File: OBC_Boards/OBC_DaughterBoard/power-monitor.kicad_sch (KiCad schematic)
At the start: 5 parts

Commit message: temp sensor footprint
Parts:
- TP2: renamed from TP?; footprint (none) -> TestPoint:TestPoint_2Pads_Pitch2.54mm_Drill0.8mm
- gave numbers to parts that had none: 4
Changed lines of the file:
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@@
   (symbol (lib_id "STM32_Breakout-rescue:MAX4372FESA+-MAX4372FESA+") (at 116.84 68.453 0) (unit 1)
     (in_bom yes) (on_board yes)
-    (property "Reference" "MAX4372F?" (id 0) (at 144.78 58.6232 0)
+    (property "Reference" "MAX4372F2" (id 0) (at 144.78 58.6232 0)
       (effects (font (size 1.524 1.524)))
     )
@@
   (symbol (lib_id "Imported_OBC_Library:+3.3V") (at 176.53 81.153 0) (mirror x) (unit 1)
     (in_bom yes) (on_board yes) (fields_autoplaced)
-    (property "Reference" "#PWR?" (id 0) (at 176.53 77.343 0)
+    (property "Reference" "#PWR0139" (id 0) (at 176.53 77.343 0)
       (effects (font (size 1.27 1.27)) hide)
     )
@@
   (symbol (lib_id "Device:R") (at 184.785 71.755 0) (unit 1)
     (in_bom yes) (on_board yes) (fields_autoplaced)
-    (property "Reference" "R?" (id 0) (at 187.325 70.4849 0)
+    (property "Reference" "R12" (id 0) (at 187.325 70.4849 0)
       (effects (font (size 1.27 1.27)) (justify left))
     )
@@
   (symbol (lib_id "power:GND") (at 141.605 127 0) (unit 1)
     (in_bom yes) (on_board yes)
-    (property "Reference" "#PWR?" (id 0) (at 141.605 133.35 0)
+    (property "Reference" "#PWR0128" (id 0) (at 141.605 133.35 0)
       (effects (font (size 1.27 1.27)) hide)
     )
@@
   (symbol (lib_id "Connector:TestPoint") (at 176.53 80.391 90) (unit 1)
     (in_bom yes) (on_board yes)
-    (property "Reference" "TP?" (id 0) (at 172.212 84.455 90)
+    (property "Reference" "TP2" (id 0) (at 172.212 84.455 90)
       (effects (font (size 1.27 1.27)) (justify left))
     )
@@
       (effects (font (size 1.27 1.27)) (justify left))
     )
-    (property "Footprint" "" (id 2) (at 176.53 75.311 0)
+    (property "Footprint" "TestPoint:TestPoint_2Pads_Pitch2.54mm_Drill0.8mm" (id 2) (at 176.53 75.311 0)
       (effects (font (size 1.27 1.27)) hide)
     )
@@
   (symbol (lib_id "Device:FerriteBead_Small") (at 91.44 68.58 270) (unit 1)
     (in_bom yes) (on_board yes)
-    (property "Reference" "FB?" (id 0) (at 89.535 62.865 90))
+    (property "Reference" "FB5" (id 0) (at 89.535 62.865 90))
     (property "Value" "100R @ 100 MHz" (id 1) (at 95.885 65.405 90))
     (property "Footprint" "Daughterboard_footprints:BEADC1608X75N" (id 2) (at 91.44 66.802 90)
@@
   (symbol (lib_id "Imported_OBC_Library:+3.3V") (at 133.985 94.615 0) (unit 1)
     (in_bom yes) (on_board yes)
-    (property "Reference" "#PWR?" (id 0) (at 133.985 98.425 0)
+    (property "Reference" "#PWR0132" (id 0) (at 133.985 98.425 0)
       (effects (font (size 1.27 1.27)) hide)
     )
@@
   (symbol (lib_id "power:GND") (at 133.985 127 0) (unit 1)
     (in_bom yes) (on_board yes)
-    (property "Reference" "#PWR?" (id 0) (at 133.985 133.35 0)
+    (property "Reference" "#PWR0127" (id 0) (at 133.985 133.35 0)
       (effects (font (size 1.27 1.27)) hide)
     )
@@
   (symbol (lib_id "Analog_ADC:MCP3008") (at 136.525 109.855 0) (unit 1)
     (in_bom yes) (on_board yes)
-    (property "Reference" "U?" (id 0) (at 110.109 112.141 0)
+    (property "Reference" "U5" (id 0) (at 110.109 112.141 0)
       (effects (font (size 1.27 1.27)) (justify left))
     )
@@
   (symbol (lib_id "power:GND") (at 107.95 79.375 0) (unit 1)
     (in_bom yes) (on_board yes)
-    (property "Reference" "#PWR?" (id 0) (at 107.95 85.725 0)
+    (property "Reference" "#PWR0137" (id 0) (at 107.95 85.725 0)
       (effects (font (size 1.27 1.27)) hide)
     )
@@
   (symbol (lib_id "Imported_OBC_Library:+3.3V") (at 86.995 59.69 0) (unit 1)
     (in_bom yes) (on_board yes)
-    (property "Reference" "#PWR?" (id 0) (at 86.995 63.5 0)
+    (property "Reference" "#PWR0138" (id 0) (at 86.995 63.5 0)
       (effects (font (size 1.27 1.27)) hide)
     )
@@
   (symbol (lib_id "Imported_OBC_Library:+3.3V") (at 141.605 94.615 0) (unit 1)
     (in_bom yes) (on_board yes)
-    (property "Reference" "#PWR?" (id 0) (at 141.605 98.425 0)
+    (property "Reference" "#PWR0136" (id 0) (at 141.605 98.425 0)
       (effects (font (size 1.27 1.27)) hide)
     )

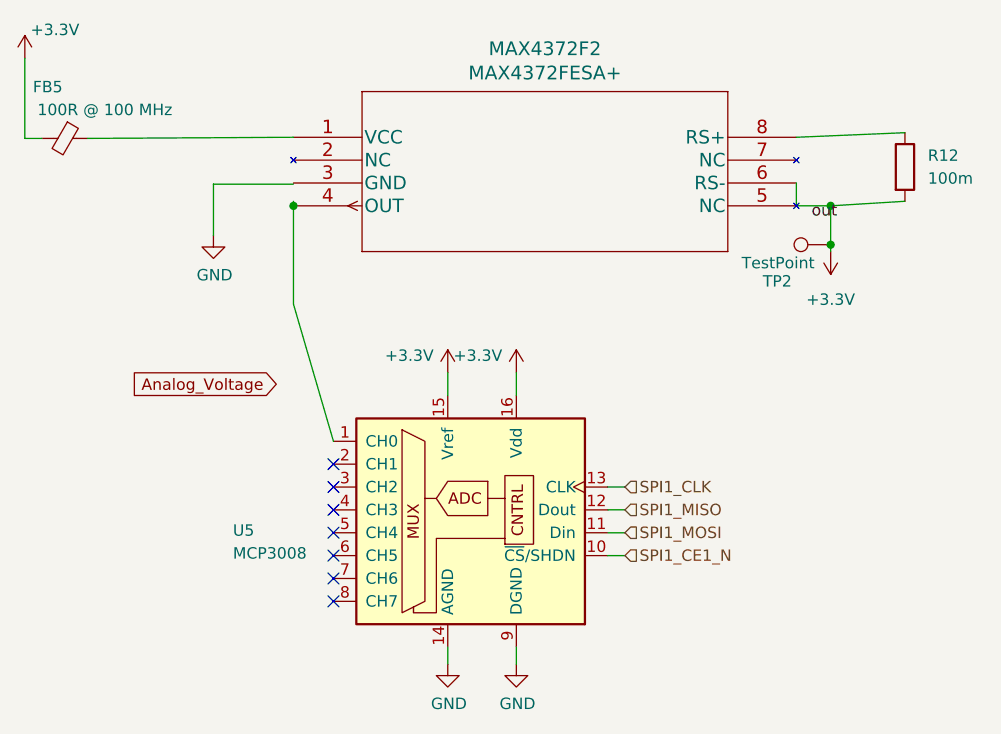
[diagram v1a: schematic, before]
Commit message: obc: daughterboard: clean up all schematics for easier reworks
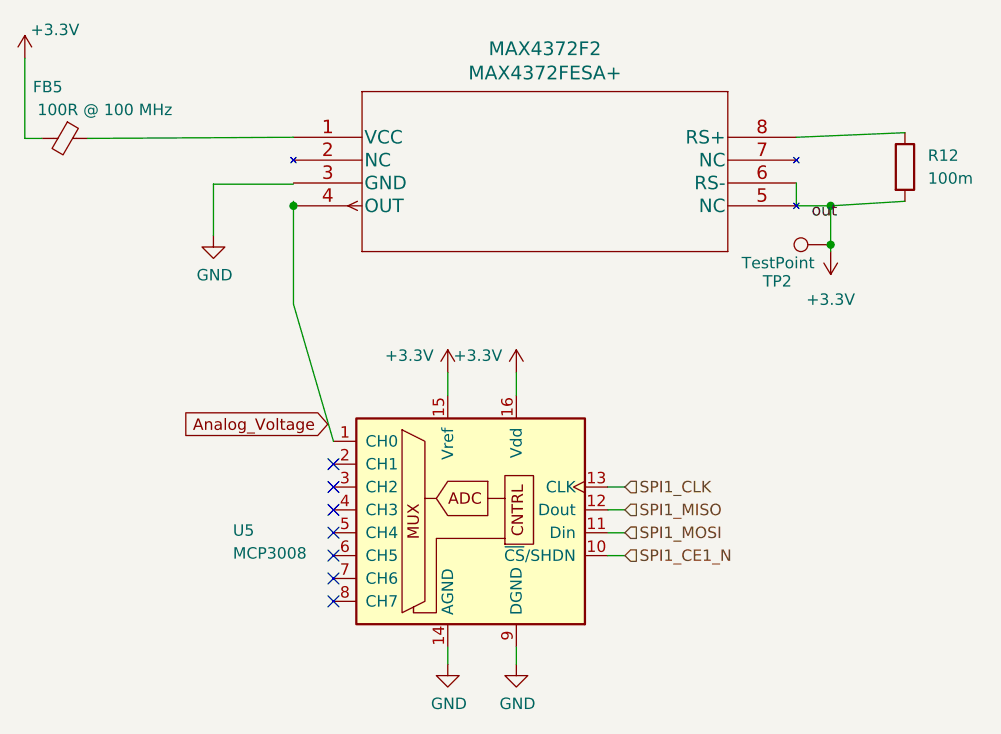
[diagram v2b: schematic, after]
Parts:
- MAX4372F2: footprint Max4372:Maxim-MAX4372FESA+-Level_A -> Daughterboard_footprints:Maxim-MAX4372FESA+-Level_A
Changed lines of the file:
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@@
     (effects (font (size 1.27 1.27)) (justify right bottom))
   )
-  (global_label "Analog_Voltage" (shape input) (at 114.935 95.885 180) (fields_autoplaced)
+  (global_label "Analog_Voltage" (shape input) (at 120.65 100.33 180) (fields_autoplaced)
     (effects (font (size 1.27 1.27)) (justify right))
-    (property "Intersheet References" "${INTERSHEET_REFS}" (id 0) (at 98.189 95.9644 0)
+    (property "Intersheet References" "${INTERSHEET_REFS}" (id 0) (at 103.904 100.4094 0)
       (effects (font (size 1.27 1.27)) (justify right) hide)
     )
@@
       (effects (font (size 1.524 1.524)))
     )
-    (property "Footprint" "Max4372:Maxim-MAX4372FESA+-Level_A" (id 2) (at 128.27 54.483 0)
+    (property "Footprint" "Daughterboard_footprints:Maxim-MAX4372FESA+-Level_A" (id 2) (at 128.27 54.483 0)
       (effects (font (size 1.524 1.524)) hide)
     )

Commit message: footprint fix
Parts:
- U5: footprint MCP3008:Microchip-MCP3008-I_P-Manufacturer_Recommended -> Daughterboard_footprints:Microchip-MCP3008-I_P-Manufacturer_Recommended
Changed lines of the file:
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@@
       (effects (font (size 1.27 1.27)) (justify left))
     )
-    (property "Footprint" "MCP3008:Microchip-MCP3008-I_P-Manufacturer_Recommended" (id 2) (at 139.065 107.315 0)
+    (property "Footprint" "Daughterboard_footprints:Microchip-MCP3008-I_P-Manufacturer_Recommended" (id 2) (at 139.065 107.315 0)
       (effects (font (size 1.27 1.27)) hide)
     )
